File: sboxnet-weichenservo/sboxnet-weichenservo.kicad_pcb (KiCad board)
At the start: 2 copper layers, 72.5 x 64.1 mm, 38 parts, among them J1 Screw_Terminal_01x02, J10 Conn_01x03_Male, J11 Conn_01x03_Male, J12 Conn_01x03_Male, J13 Conn_02x08_Top_Bottom, J2 Screw_Terminal_01x04, J3 Conn_02x17_Odd_Even, J4 Screw_Terminal_01x04, J5 Conn_01x03_Male, J6 Conn_01x03_Male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

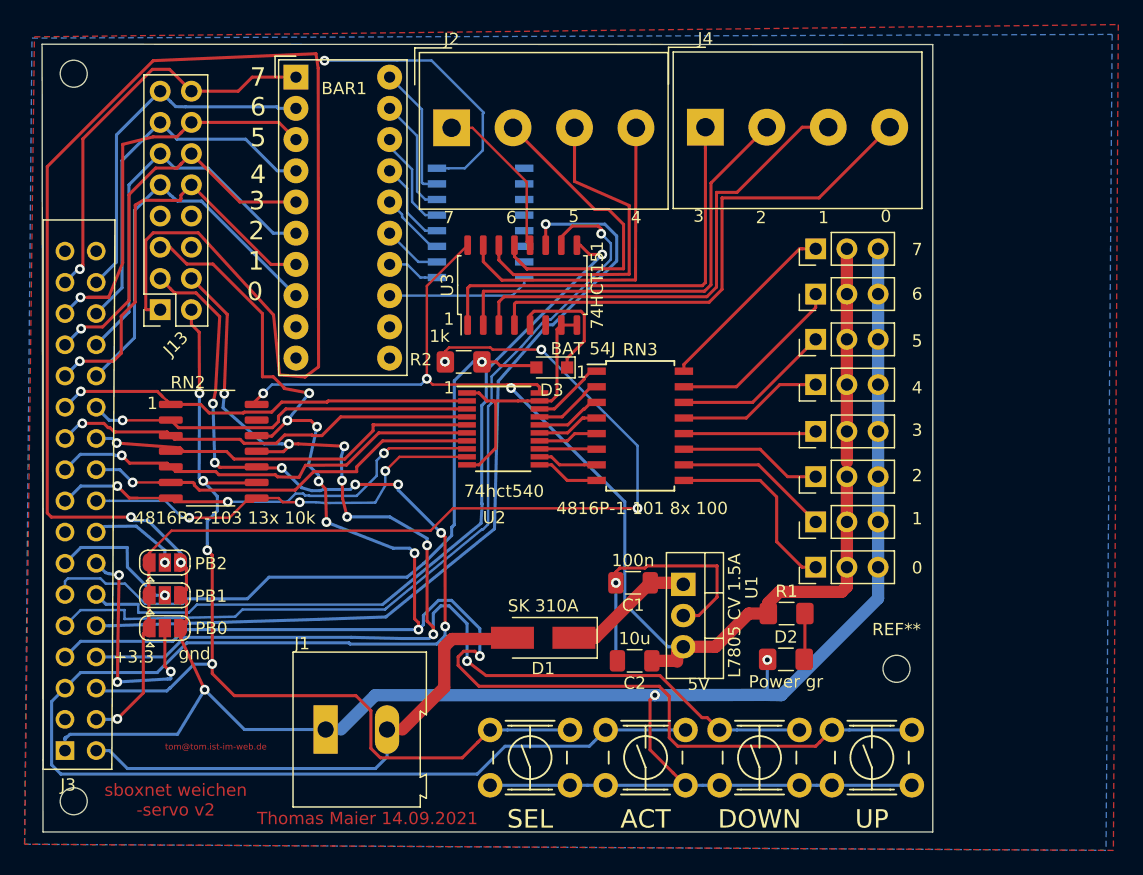
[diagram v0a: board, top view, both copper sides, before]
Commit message: weichenservo mit PBx und Rueckmeldung pull up
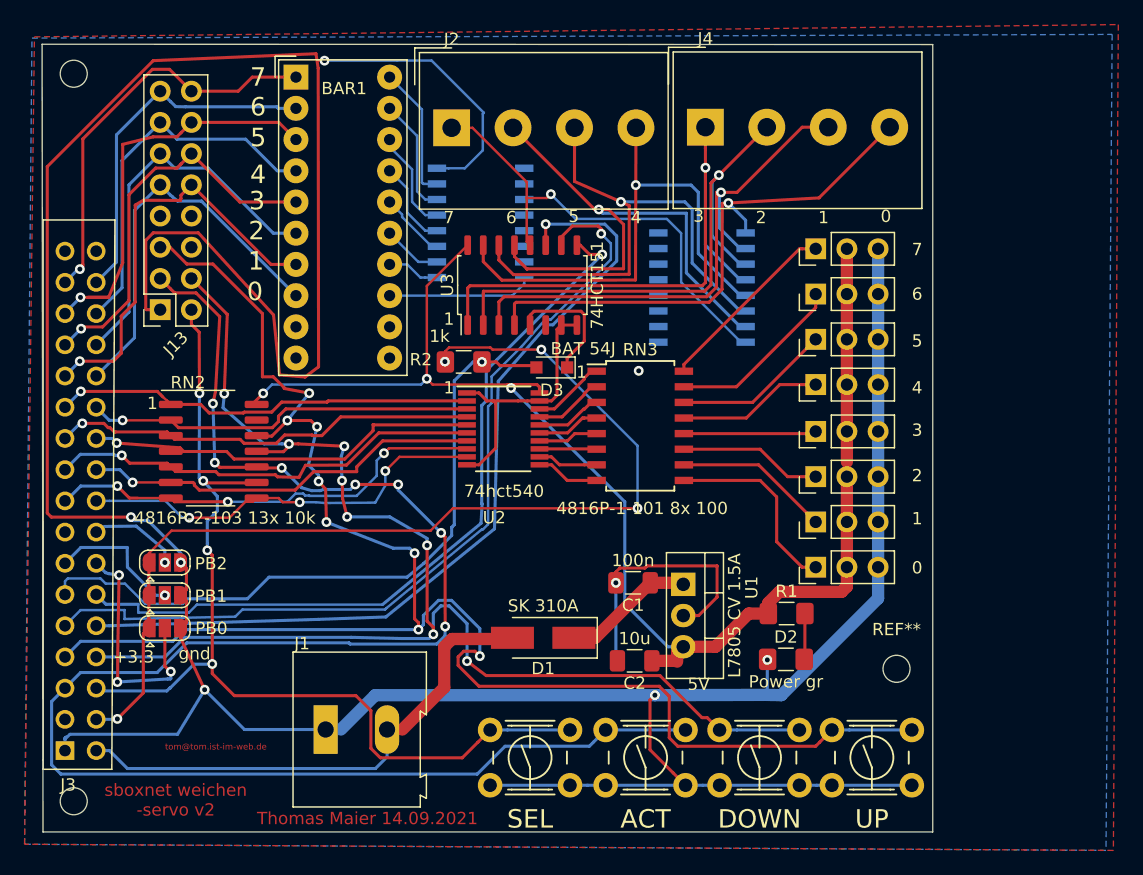
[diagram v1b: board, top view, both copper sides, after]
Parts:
- added RN5: 4816P-T02-103 15x1k, Package_SO:SOIC-16W_5.3x10.2mm_P1.27mm, B.Cu at (70.1, 125.2)
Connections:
- net Net-(J2-Pad1) renamed /a8
- net Net-(J2-Pad2) renamed /a7
- net Net-(J2-Pad3) renamed /a6
- net Net-(J2-Pad4) renamed /a5
- net Net-(J4-Pad1) renamed /a4
- net Net-(J4-Pad2) renamed /a3
- net Net-(J4-Pad3) renamed /a2
- net Net-(J4-Pad4) renamed /a1
- BAR1 pad 10: Net-(BAR1-Pad10) -> unconnected-(BAR1-Pad10)
- BAR1 pad 11: Net-(BAR1-Pad11) -> unconnected-(BAR1-Pad11)
- BAR1 pad 12: Net-(BAR1-Pad12) -> unconnected-(BAR1-Pad12)
- BAR1 pad 9: Net-(BAR1-Pad9) -> unconnected-(BAR1-Pad9)
- J13 pad 6: Net-(J13-Pad6) -> unconnected-(J13-Pad6)
- J13 pad 7: Net-(J13-Pad7) -> unconnected-(J13-Pad7)
- J13 pad 8: Net-(J13-Pad8) -> unconnected-(J13-Pad8)
- J3 pad 16: Net-(J3-Pad16) -> unconnected-(J3-Pad16)
- J3 pad 33: Net-(J3-Pad33) -> unconnected-(J3-Pad33)
- J3 pad 34: Net-(J3-Pad34) -> unconnected-(J3-Pad34)
- J3 pad 4: Net-(J3-Pad4) -> unconnected-(J3-Pad4)
- RN1 pad 1: Net-(RN1-Pad1) -> unconnected-(RN1-Pad1)
- RN1 pad 2: Net-(RN1-Pad2) -> unconnected-(RN1-Pad2)
- RN1 pad 3: Net-(RN1-Pad3) -> unconnected-(RN1-Pad3)
- RN1 pad 4: Net-(RN1-Pad4) -> unconnected-(RN1-Pad4)
- RN1 pad 5: Net-(RN1-Pad5) -> unconnected-(RN1-Pad5)
- RN1 pad 6: Net-(RN1-Pad6) -> unconnected-(RN1-Pad6)
- RN1 pad 7: Net-(RN1-Pad7) -> unconnected-(RN1-Pad7)
- RN2 pad 13: Net-(RN2-Pad13) -> unconnected-(RN2-Pad13)
- U3 pad 6: Net-(U3-Pad6) -> unconnected-(U3-Pad6)
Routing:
- net /a8: track 13.2 -> 38.5 mm, vias 0 -> 1
- net /a7: track 26.1 -> 44.8 mm, vias 0 -> 1
- net /a6: track 27.1 -> 43.5 mm, vias 0 -> 1
- net /a5: track 26.7 -> 42.3 mm, vias 0 -> 1
- net /a4: track 35.2 -> 45.9 mm, vias 0 -> 1
- net /a3: track 36.2 -> 45.1 mm, vias 0 -> 1
- net /a2: track 39.1 -> 44.9 mm, vias 0 -> 1
- net /a1: track 42.6 -> 45.1 mm, vias 0 -> 1
- net GND: vias 7 -> 8
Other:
- net class Default removed
